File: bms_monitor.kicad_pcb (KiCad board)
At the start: 2 copper layers, 115 x 65 mm, 243 parts, among them CN1 10nF, CN10 10nF, CN11 10nF, CN12 10nF, CN13 10nF, CN14 10nF, CN2 10nF, CN3 10nF, CN4 10nF, CN5 10nF, CN6 10nF, CN7 10nF, CN8 10nF, CN9 10nF, J1 Conn_01x02, J10 TEMP0, J11 TEMP1, J12 Conn_01x05, J14 5V, J15 Conn_ST_STDC14, J2 Conn_01x02, J3 Conn_01x02, J4 Conn_01x02, J5 CELLS, J6 TEMP0, J7 TEMP1, J8 Conn_01x05, J9 CELLS, Q1 NSV1C201MZ4, Q2 NSV1C201MZ4, U1 STM32L432KBUx, U10 CD74HC4067SM, U11 MP4541, U12 SM91502ALA, U13 SM91502ALA, U14 SM91502ALA, U3 DSC61XX, U4 TFBS4652, U5 LTC6811-1, U6 CD74HC4067SM, U7 MP4541, U8 SM91502ALA, U9 LTC6811-1

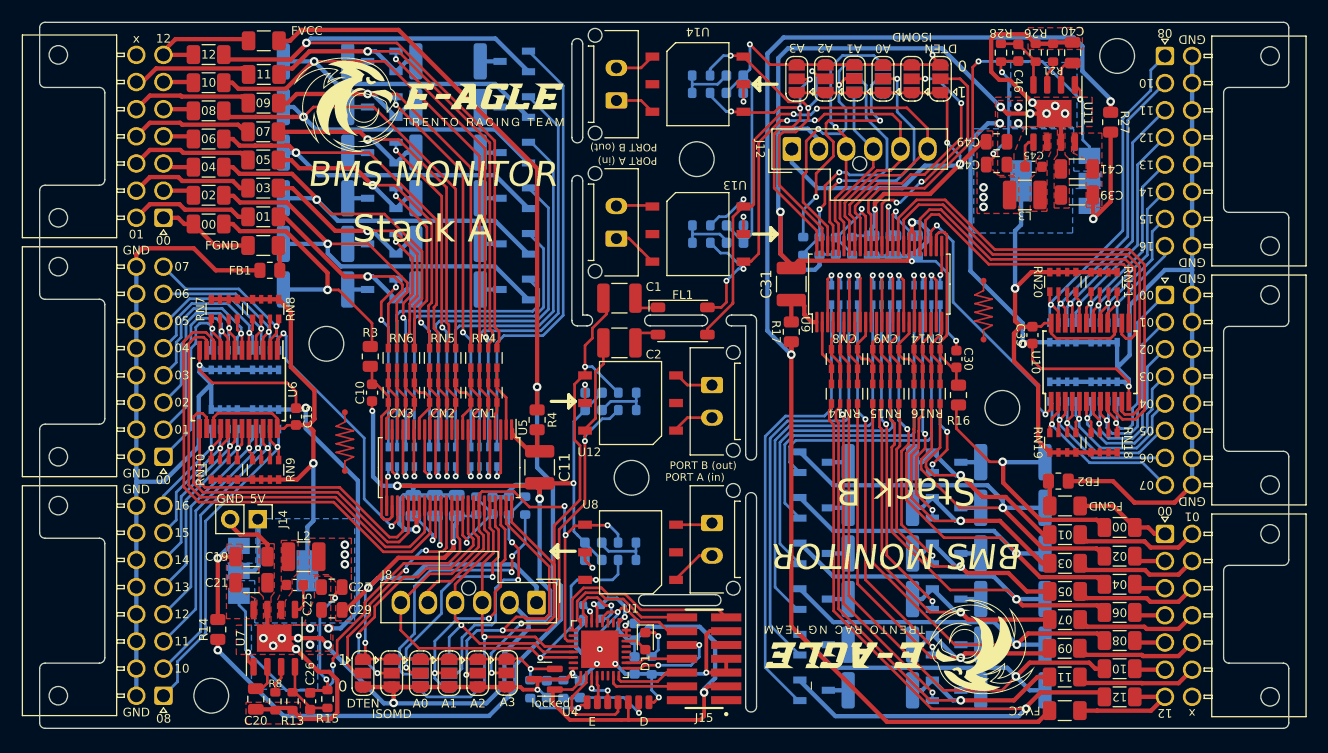
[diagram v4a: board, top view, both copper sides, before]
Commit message: fix
added ltc gpio pull up resistor
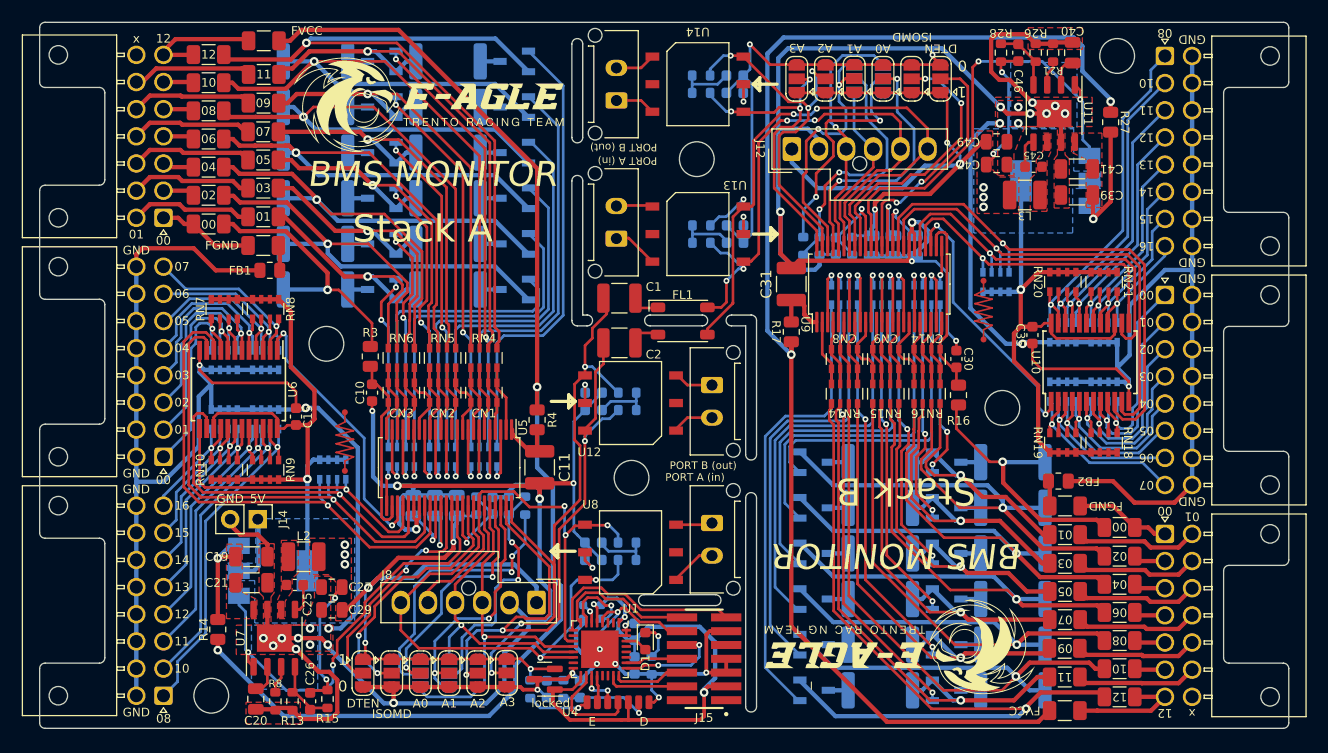
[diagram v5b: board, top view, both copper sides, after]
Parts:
- added RN17: 10K, Resistor_SMD:R_Array_Convex_4x0603, B.Cu at (107.0, 103.2)
- added RN22: 10K, Resistor_SMD:R_Array_Convex_4x0603, B.Cu at (168.0, 85.9)
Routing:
- net +5V: track 140.6 -> 144.0 mm
- net /StackB/VCC: track 126.6 -> 129.2 mm
- net /StackB/MUX_A0: track 46.1 -> 48.7 mm, vias 0 -> 1
- net /StackA/MUX_A0: track 46.1 -> 48.5 mm, vias 0 -> 1
- net /StackB/MUX_A1: track 43.0 -> 45.1 mm, vias 0 -> 1
- net /StackA/MUX_A1: track 43.0 -> 44.7 mm, vias 0 -> 1
- net /StackB/MUX_A2: track 33.5 -> 34.7 mm, vias 0 -> 1
- net /StackA/MUX_A2: track 33.5 -> 34.6 mm, vias 0 -> 1
- net /StackB/GND: track 287.2 -> 288.1 mm
- net /StackB/MUX_A3: track 28.3 -> 29.0 mm, vias 0 -> 1
- net GND: track 323.7 -> 324.4 mm
- net /StackA/MUX_A3: track 28.3 -> 28.7 mm, vias 0 -> 1

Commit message: fabrication
added fabrication files
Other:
- board text added: "2"
- board text added: "3"
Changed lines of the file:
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@@
     (property "Sheetname" "StackA")
     (attr exclude_from_pos_files)
-    (fp_text reference "JP14" (at 2.5908 0) (layer "B.SilkS")
+    (fp_text reference "JP14" (at 2.7178 0) (layer "B.SilkS")
       (effects (font (size 0.8 0.8) (thickness 0.15)) (justify mirror))
     )
@@
     (property "Sheetname" "StackB")
     (attr exclude_from_pos_files)
-    (fp_text reference "JP16" (at 2.6416 -0.0155) (layer "B.SilkS")
+    (fp_text reference "JP16" (at 2.7178 -0.0409 180 unlocked) (layer "B.SilkS")
       (effects (font (size 0.8 0.8) (thickness 0.15)) (justify mirror))
     )
@@
     (property "Sheetname" "StackB")
     (attr exclude_from_pos_files)
-    (fp_text reference "JP15" (at -2.7686 0.0254) (layer "B.SilkS")
+    (fp_text reference "JP15" (at -2.794 0.0353 180 unlocked) (layer "B.SilkS")
       (effects (font (size 0.8 0.8) (thickness 0.15)) (justify mirror))
     )
@@
     (effects (font (size 2 2) (thickness 0.3)) (justify mirror))
   )
+  (gr_text "1" (at 153.3398 65.913 180) (layer "B.SilkS")
+    (effects (font (size 0.8 0.8) (thickness 0.15)) (justify mirror))
+  )
   (gr_text "TDI" (at 139.0904 119.3292) (layer "B.SilkS")
     (effects (font (size 0.7 0.7) (thickness 0.12)) (justify mirror))
@@
     (effects (font (size 0.8 0.8) (thickness 0.12)) (justify mirror))
   )
+  (gr_text "2\n" (at 153.3652 67.1068 180) (layer "B.SilkS")
+    (effects (font (size 0.8 0.8) (thickness 0.15)) (justify mirror))
+  )
   (gr_text "14" (at 93.1 109) (layer "B.SilkS")
     (effects (font (size 0.8 0.8) (thickness 0.12)) (justify mirror))
@@
     (effects (font (size 0.8 0.8) (thickness 0.12)) (justify mirror))
   )
+  (gr_text "1" (at 119.38 123.1138) (layer "B.SilkS")
+    (effects (font (size 0.8 0.8) (thickness 0.15)) (justify mirror))
+  )
   (gr_text "13" (at 181.9 77.6 -180) (layer "B.SilkS")
     (effects (font (size 0.8 0.8) (thickness 0.12)) (justify mirror))
@@
     (effects (font (size 0.8 0.8) (thickness 0.12)) (justify mirror))
   )
+  (gr_text "3" (at 119.3546 120.6754) (layer "B.SilkS")
+    (effects (font (size 0.8 0.8) (thickness 0.15)) (justify mirror))
+  )
   (gr_text "R_{n}" (at 117 92.5) (layer "B.SilkS")
     (effects (font (size 0.8 0.8) (thickness 0.12)) (justify mirror))
@@
     (effects (font (size 0.8 0.8) (thickness 0.12)) (justify mirror))
   )
+  (gr_text "3" (at 153.3652 68.3514 180) (layer "B.SilkS")
+    (effects (font (size 0.8 0.8) (thickness 0.15)) (justify mirror))
+  )
   (gr_text "GND" (at 123.3 114.3 270) (layer "B.SilkS")
     (effects (font (size 0.8 0.8) (thickness 0.12)) (justify left mirror))
@@
     (effects (font (size 0.8 0.8) (thickness 0.12)) (justify mirror))
   )
+  (gr_text "2\n" (at 119.3546 121.92) (layer "B.SilkS")
+    (effects (font (size 0.8 0.8) (thickness 0.15)) (justify mirror))
+  )
   (gr_text "06" (at 93.1 87) (layer "F.SilkS")
     (effects (font (size 0.8 0.8) (thickness 0.12)))
@@
   (segment (start 107.055804 105.948551) (end 106.5848 105.477547) (width 0.25) (layer "B.Cu") (net 205))
   (segment (start 106.5848 105.477547) (end 106.5848 104.0748) (width 0.25) (layer "B.Cu") (net 205))
-  (segment (start 106.2474 104.825) (end 108.04236 104.825) (width 0.25) (layer "F.Cu") (net 206))
+  (segment (start 95.225 104.825) (end 108.04236 104.825) (width 0.25) (layer "F.Cu") (net 206))
   (segment (start 94.725 99.4) (end 94.725 104.325) (width 0.25) (layer "F.Cu") (net 206))
   (segment (start 108.04236 104.825) (end 112.134195 108.916835) (width 0.25) (layer "F.Cu") (net 206))
   (segment (start 112.134195 108.916835) (end 113.028365 108.916835) (width 0.25) (layer "F.Cu") (net 206))
-  (segment (start 106.242 104.8196) (end 106.2474 104.825) (width 0.25) (layer "F.Cu") (net 206))
   (segment (start 94.725 104.325) (end 95.225 104.825) (width 0.25) (layer "F.Cu") (net 206))
   (segment (start 113.028365 108.916835) (end 113.45 108.4952) (width 0.25) (layer "F.Cu") (net 206))
   (segment (start 113.45 108.4952) (end 113.45 106.5) (width 0.25) (layer "F.Cu") (net 206))
-  (segment (start 95.225 104.825) (end 106.2474 104.825) (width 0.25) (layer "F.Cu") (net 206))
   (via (at 108.240485 105.018154) (size 0.55) (drill 0.25) (layers "F.Cu" "B.Cu") (net 206))
   (segment (start 108.240485 105.018154) (end 108.1848 104.962469) (width 0.25) (layer "B.Cu") (net 206))

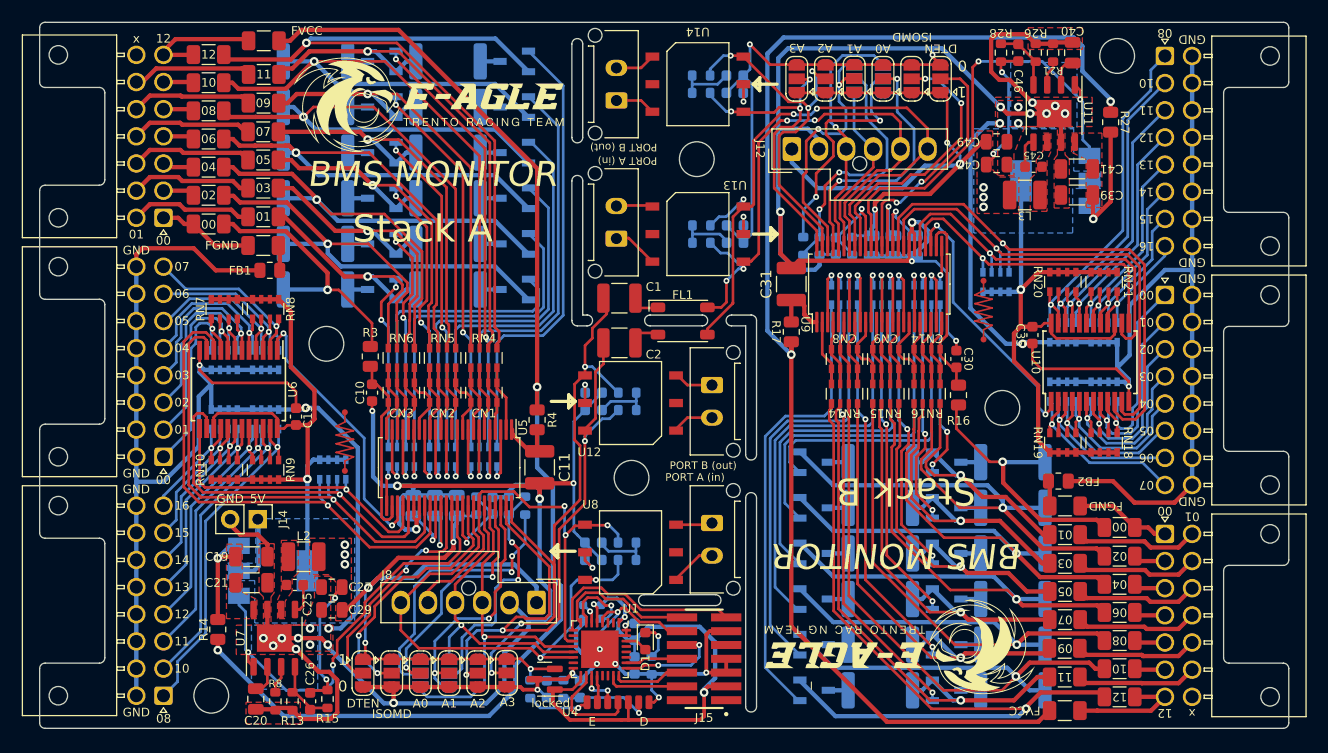
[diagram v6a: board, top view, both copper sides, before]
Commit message: fix
- added pmos for reverse polarity protection to prog pwr
- fixed temp connectors numbering (silkscreen)
- regenerated fabrication files
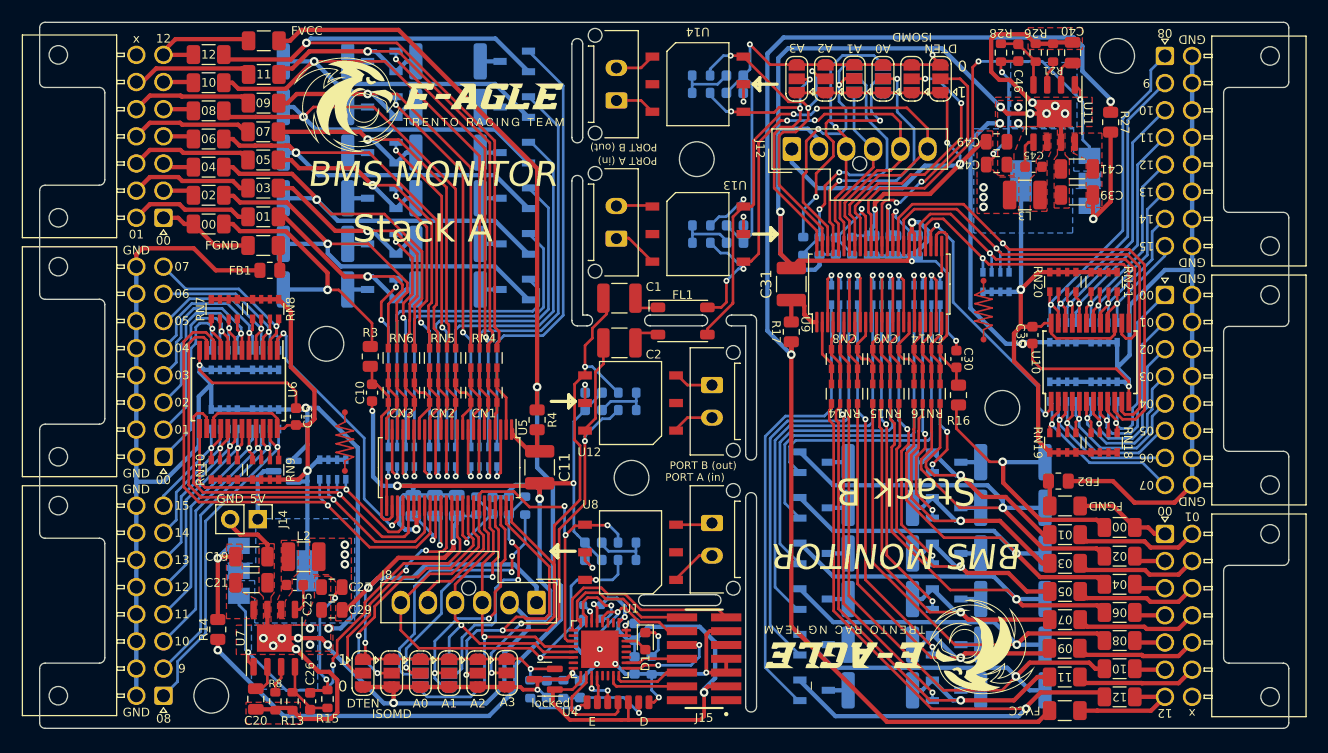
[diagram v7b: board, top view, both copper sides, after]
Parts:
- added Q3: PMV65XP, Package_TO_SOT_SMD:SOT-23, B.Cu at (102.5, 103.3)
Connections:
- J14 pad 1: +5V -> Net-(J14-Pad1)
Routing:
- net Net-(J14-Pad1): track 0.00 -> 5.54 mm
- net +5V: track 144.0 -> 138.5 mm
- net GND: track 324.4 -> 329.8 mm
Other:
- board text added: "9"
- board text removed: "16"

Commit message: fab: update pcb for fabrication
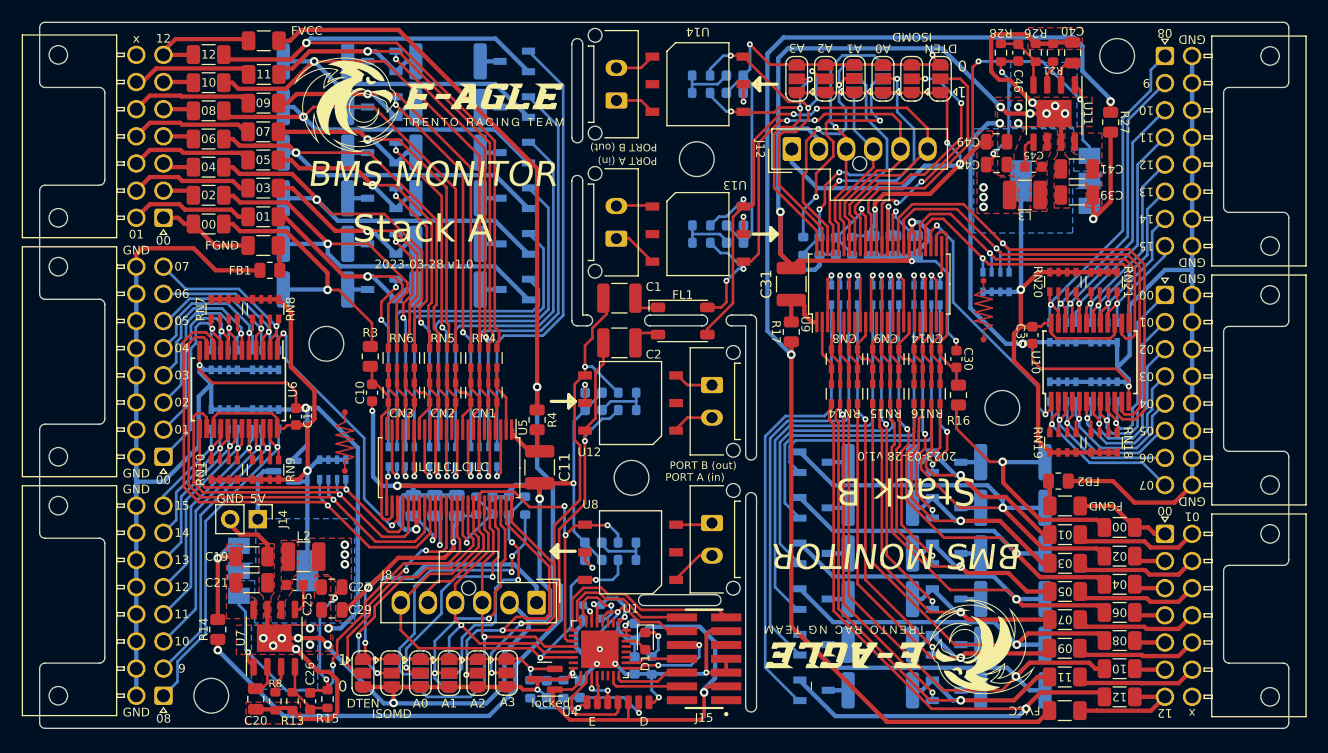
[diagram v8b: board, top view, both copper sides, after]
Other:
- board text added: "2023-03-28 v1.0"
- board text added: "JLCJLCJLCJLC"
